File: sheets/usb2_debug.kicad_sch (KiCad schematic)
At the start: 10 parts, among them J3 TYPE-C-31-M-12, U8 TS3USB221DRCR

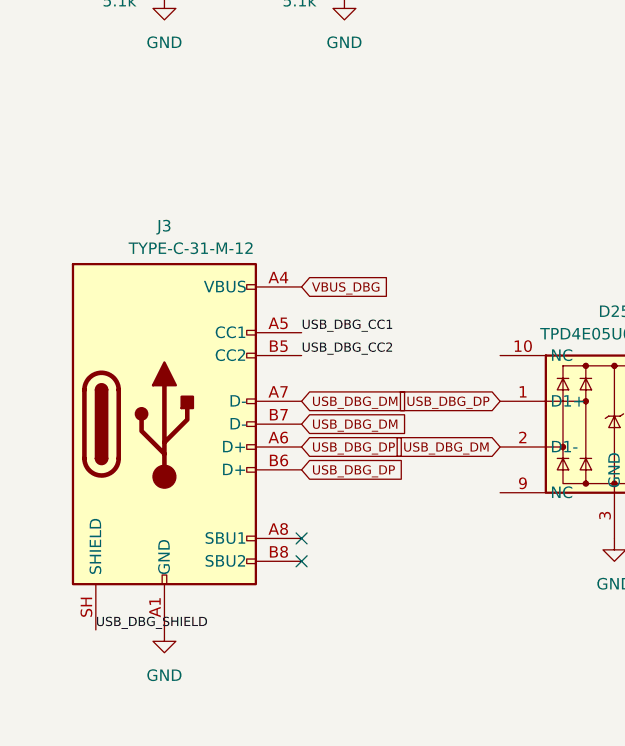
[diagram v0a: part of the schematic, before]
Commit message: sch: consolidate USB-C to TYPE-C-31-M-04 x3, re-pick SIM socket with verified CAD
Co-Authored-By: Claude Fable 5 <noreply@anthropic.com>
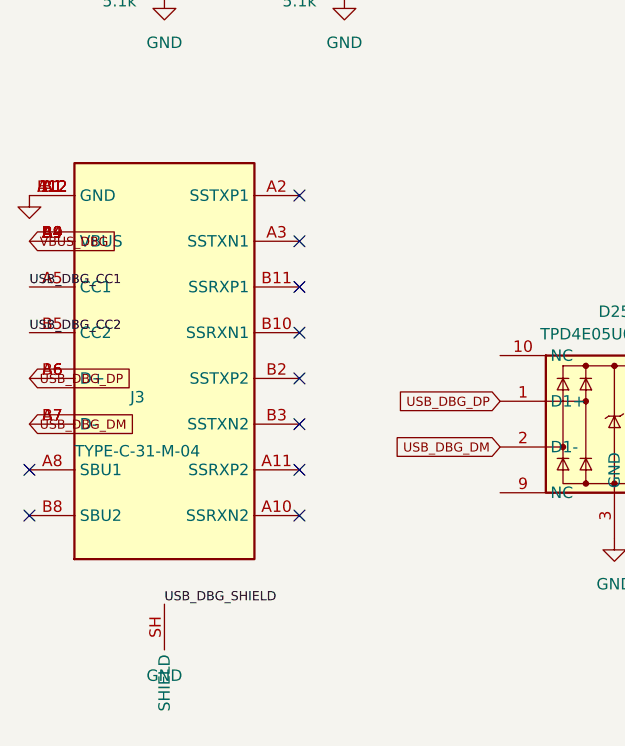
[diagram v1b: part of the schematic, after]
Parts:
- J3: value TYPE-C-31-M-12 -> TYPE-C-31-M-04; footprint Connector_USB:USB_C_Receptacle_HRO_TYPE-C-31-M-12 -> sierra-to-usb:USB_C_Receptacle_HRO_TYPE-C-31-M-04; symbol Connector:USB_C_Receptacle_USB2.0_16P -> sierra-to-usb:USB_C_Receptacle_USB3.2_24P; LCSC C165948 -> C129018; MPN HRO TYPE-C-31-M-12 -> HRO TYPE-C-31-M-04
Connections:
- no-connect marks 4 -> 12
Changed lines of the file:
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@@
 	(paper "A4")
 	(no_connect
-		(at 35.24 112.7)
+		(at 35 74.6)
+	)
+	(no_connect
+		(at 35 79.68)
+	)
+	(no_connect
+		(at 35 84.76)
+	)
+	(no_connect
+		(at 35 89.84)
+	)
+	(no_connect
+		(at 35 94.92)
+	)
+	(no_connect
+		(at 35 100)
+	)
+	(no_connect
+		(at 35 105.08)
+	)
+	(no_connect
+		(at 35 110.16)
+	)
+	(no_connect
+		(at 5 105.08)
 	)
 	(no_connect
@@
 	)
 	(no_connect
-		(at 35.24 115.24)
+		(at 5 110.16)
 	)
 	(no_connect
@@
 	)
 	(label "USB_DBG_CC1"
-		(at 35.24 89.84 0)
+		(at 5 84.76 0)
 		(effects
 			(font
@@
 	)
 	(label "USB_DBG_CC2"
-		(at 35.24 92.38 0)
+		(at 5 89.84 0)
 		(effects
 			(font
@@
 	)
 	(label "USB_DBG_SHIELD"
-		(at 12.38 122.86 0)
+		(at 20 120 0)
 		(effects
 			(font
@@
 	(global_label "USB_DBG_DP"
 		(shape input)
-		(at 35.24 102.54 0)
+		(at 5 94.92 0)
 		(effects
 			(font
@@
 		)
 		(property "Intersheetrefs" "${INTERSHEET_REFS}"
-			(at 35.24 102.54 0)
-			(show_name no)
-			(do_not_autoplace no)
-			(effects
-				(font
-					(size 1.27 1.27)
-				)
-			)
-		)
-	)
-	(global_label "USB_DBG_DP"
-		(shape input)
-		(at 35.24 105.08 0)
-		(effects
-			(font
-				(size 1.016 1.016)
-			)
-			(justify left bottom)
-		)
-		(property "Intersheetrefs" "${INTERSHEET_REFS}"
-			(at 35.24 105.08 0)
+			(at 5 94.92 0)
 			(show_name no)
 			(do_not_autoplace no)
@@
 	(global_label "USB_DBG_DM"
 		(shape input)
-		(at 35.24 97.46 0)
+		(at 5 100 0)
 		(effects
 			(font
@@
 		)
 		(property "Intersheetrefs" "${INTERSHEET_REFS}"
-			(at 35.24 97.46 0)
-			(show_name no)
-			(do_not_autoplace no)
-			(effects
-				(font
-					(size 1.27 1.27)
-				)
-			)
-		)
-	)
-	(global_label "USB_DBG_DM"
-		(shape input)
-		(at 35.24 100 0)
-		(effects
-			(font
-				(size 1.016 1.016)
-			)
-			(justify left bottom)
-		)
-		(property "Intersheetrefs" "${INTERSHEET_REFS}"
-			(at 35.24 100 0)
+			(at 5 100 0)
 			(show_name no)
 			(do_not_autoplace no)
@@
 	(global_label "VBUS_DBG"
 		(shape input)
-		(at 35.24 84.76 0)
+		(at 5 79.68 0)
 		(effects
 			(font
@@
 		)
 		(property "Intersheetrefs" "${INTERSHEET_REFS}"
-			(at 35.24 84.76 0)
+			(at 5 79.68 0)
 			(show_name no)
 			(do_not_autoplace no)
@@
 	(symbol
 		(lib_id "power:GND")
-		(at 20 122.86 0)
+		(at 5 74.6 0)
 		(unit 1)
 		(body_style 1)
@@
 		)
 		(property "Footprint" ""
-			(at 20 122.86 0)
+			(at 5 74.6 0)
 			(hide yes)
 			(show_name no)
@@
 		)
 		(property "Datasheet" ""
-			(at 20 122.86 0)
+			(at 5 74.6 0)
 			(hide yes)
 			(show_name no)
@@
 		)
 		(property "Description" ""
-			(at 20 122.86 0)
+			(at 5 74.6 0)
 			(show_name no)
 			(do_not_autoplace no)
@@
 	)
 	(symbol
-		(lib_id "Connector:USB_C_Receptacle_USB2.0_16P")
+		(lib_id "sierra-to-usb:USB_C_Receptacle_USB3.2_24P")
 		(at 20 100 0)
 		(unit 1)
@@
 		(fields_autoplaced yes)
 		(property "Reference" "J3"
-			(at 20 78 0)
-			(show_name no)
-			(do_not_autoplace no)
-			(effects
-				(font
-					(size 1.27 1.27)
-				)
-			)
-		)
-		(property "Value" "TYPE-C-31-M-12"
-			(at 23 80.5 0)
-			(show_name no)
-			(do_not_autoplace no)
-			(effects
-				(font
-					(size 1.27 1.27)
-				)
-			)
-		)
-		(property "Footprint" "Connector_USB:USB_C_Receptacle_HRO_TYPE-C-31-M-12"
+			(at 17 97 0)
+			(show_name no)
+			(do_not_autoplace no)
+			(effects
+				(font
+					(size 1.27 1.27)
+				)
+			)
+		)
+		(property "Value" "TYPE-C-31-M-04"
+			(at 17 103 0)
+			(show_name no)
+			(do_not_autoplace no)
+			(effects
+				(font
+					(size 1.27 1.27)
+				)
+			)
+		)
+		(property "Footprint" "sierra-to-usb:USB_C_Receptacle_HRO_TYPE-C-31-M-04"
 			(at 20 100 0)
 			(hide yes)
@@
 			)
 		)
-		(property "Datasheet" ""
+		(property "Datasheet" "https://datasheet.lcsc.com/datasheet/pdf/c25d4978cafd1404c08bb98baca46f59.pdf"
 			(at 20 100 0)
 			(hide yes)
@@
 			)
 		)
-		(property "LCSC" "C165948"
+		(property "LCSC" "C129018"
 			(at 20 100 0)
 			(hide yes)
@@
 			)
 		)
-		(property "MPN" "HRO TYPE-C-31-M-12"
+		(property "MPN" "HRO TYPE-C-31-M-04"
 			(at 20 100 0)
 			(hide yes)
@@
 		(pin "A1"
 		)
+		(pin "A12"
+		)
+		(pin "B1"
+		)
+		(pin "B12"
+		)
 		(pin "A4"
 		)
+		(pin "A9"
+		)
+		(pin "B4"
+		)
+		(pin "B9"
+		)
 		(pin "A5"
 		)
+		(pin "B5"
+		)
 		(pin "A6"
 		)
+		(pin "B6"
+		)
 		(pin "A7"
 		)
+		(pin "B7"
+		)
 		(pin "A8"
 		)
-		(pin "A9"
-		)
-		(pin "A12"
-		)
-		(pin "B1"
-		)
-		(pin "B4"
-		)
-		(pin "B5"
-		)
-		(pin "B6"
-		)
-		(pin "B7"
-		)
 		(pin "B8"
 		)
-		(pin "B9"
-		)
-		(pin "B12"
+		(pin "A2"
+		)
+		(pin "A3"
+		)
+		(pin "B11"
+		)
+		(pin "B10"
+		)
+		(pin "B2"
+		)
+		(pin "B3"
+		)
+		(pin "A11"
+		)
+		(pin "A10"
 		)
 		(pin "SH"

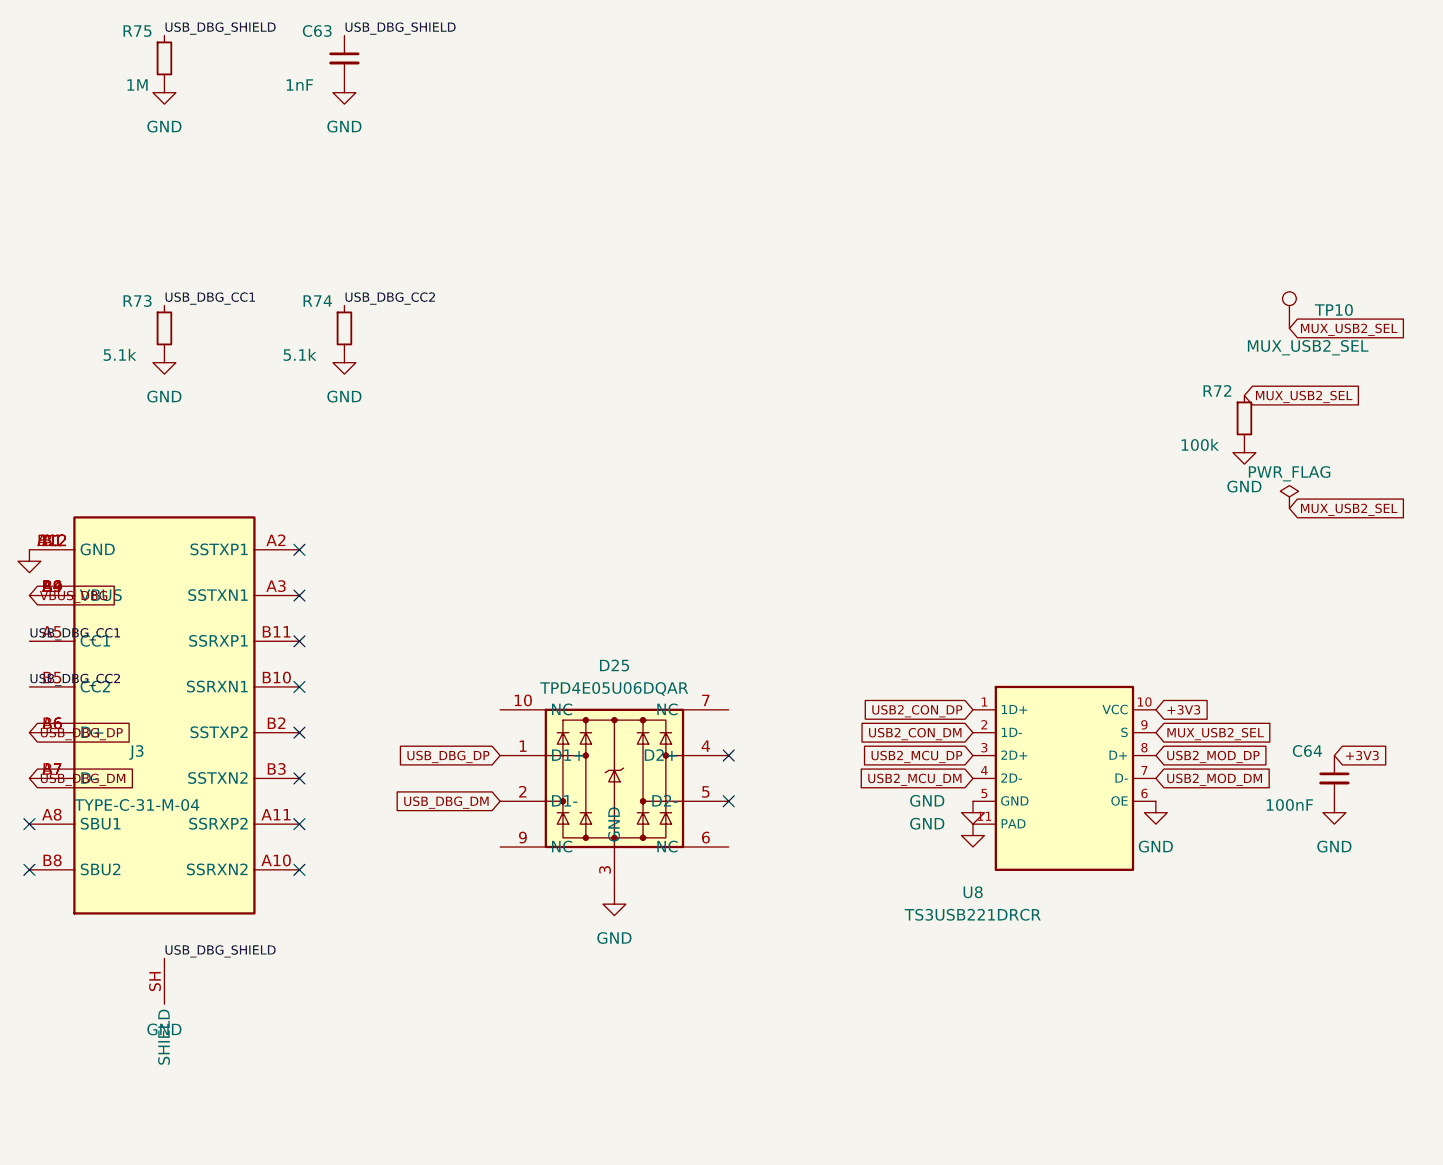
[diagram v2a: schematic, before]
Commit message: sch: finish USB-C symbol-swap rework, fix grid-snap shorts + BR pinout
User rework completed: J1/J3 (Connector:USB_C_Receptacle) rewired to their
HEAD net maps (J1 nudged on-grid), J2 PD data lines (R98/R83 -> CH224K
DP/DM) locked into netchecks, MDB10S bridges relabeled so +/- feed
POE_VDD54/POE_VSS and ~ pins take POE_VA/VB pairs, C58/C59 moved off
U1's CC2/TX2P/RX2P pins (grid-snap had stacked their pin ends), R79
moved off R78.2's node (same failure mode), CH224K_VDD flag-farm label
renamed, USB2_MOD_D+/- reverted to canonical USB2_MOD_DP/DM, stale
debris labels and orphan GND symbols deleted.

check_nets: all pass. ERC: 0. Netlist diff vs HEAD = intentional only.

Co-Authored-By: Claude Fable 5 <noreply@anthropic.com>
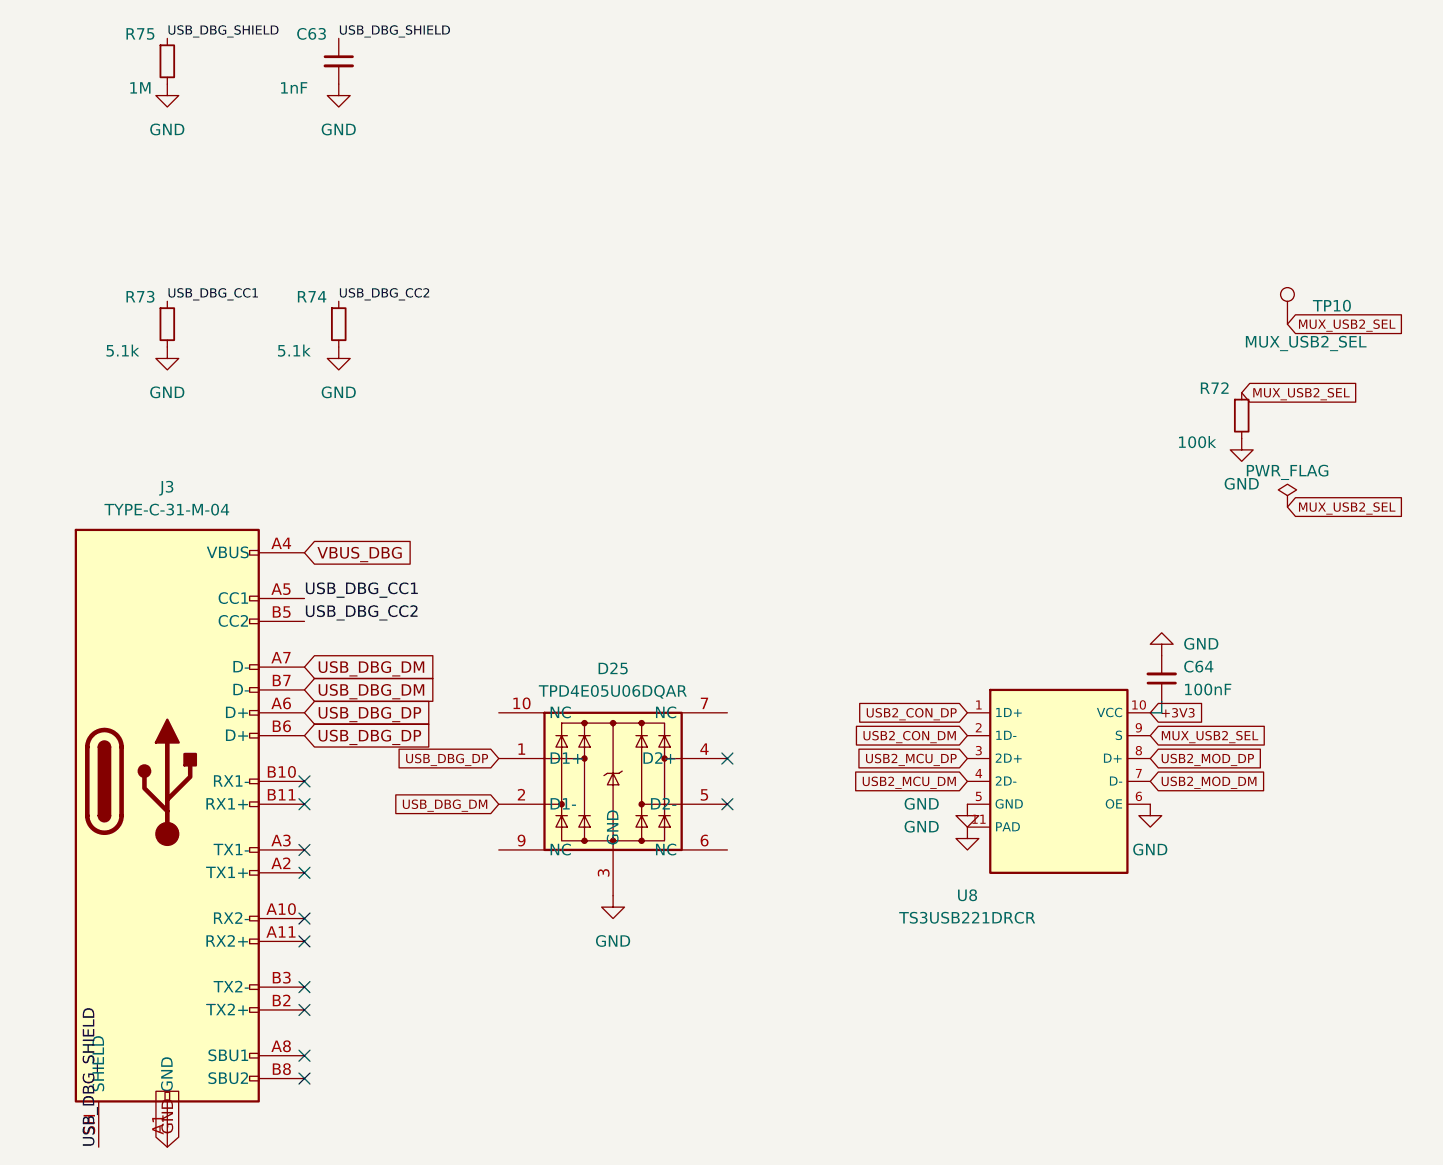
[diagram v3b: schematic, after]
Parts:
- C63, C64, R72, R73, R74, R75: KiLib_Generator (none) -> SMD_2terminal_chip_molded
- J3: symbol sierra-to-usb:USB_C_Receptacle_USB3.2_24P -> Connector:USB_C_Receptacle; LCSC Part (none) -> C129018
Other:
- company: (none) -> Alex Gompper
- title: (none) -> M.2 5G Modem Carrier
- moved on the sheet: C63, C64, R73, R74, TP10, U8
